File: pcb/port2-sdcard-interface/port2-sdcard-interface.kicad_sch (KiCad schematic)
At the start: 55 parts, among them J2 P2000T Port 2, J3 SD Card, U1 CY62128ELL-45SXI, U10 74HC32, U11 74HC273, U12 74HC165, U13 74HC595, U14 74HC00, U15 SST39SF010, U17 74HC138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

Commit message: LEDs and improved SD card assembly rountines (#2)
* Adding secondary LEDs

* Fixing bug in erroneously triggered LEDs

* Fixing bug in RAM/ROM leds

* Update config.h

* Adding LEDs in software and improvSD card assembly routines
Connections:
- net ~{RD}: no longer U9.5
- net ~{S2}: no longer U9.4
- net ~{S5}: now also U9.4; no longer U4.12, U4.13
- net ~{WR}: now also U9.5
- net at U9.6: now also U4.12, U4.13
- no-connect marks 27 -> 26
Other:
- moved on the sheet: U4D, U9B
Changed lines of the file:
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@@
   (title_block
     (title "Philips P2000T SD-CARD SLOT2 cartridge")
-    (date "2024-01-21")
-    (rev "rev1")
+    (date "2024-03-25")
+    (rev "rev3")
   )
     (symbol "Device:C" (pin_numbers hide) (pin_names (offset 0.254)) (in_bom yes) (on_board yes)
@@
     )
   )
-  (junction (at 142.875 146.685) (diameter 0) (color 0 0 0 0)
-  )
   (junction (at 48.895 203.835) (diameter 0) (color 0 0 0 0)
   )
@@
   (junction (at 35.56 222.885) (diameter 0) (color 0 0 0 0)
   )
+  (junction (at 148.59 149.86) (diameter 0) (color 0 0 0 0)
+  )
   (junction (at 90.17 203.835) (diameter 0) (color 0 0 0 0)
   )
@@
   (no_connect (at 92.71 149.86))
   (no_connect (at 50.165 111.76))
-  (no_connect (at 127 104.14))
   (no_connect (at 50.165 114.3))
   (no_connect (at 90.17 41.275))
@@
     (stroke (width 0) (type default))
   )
-  (wire (pts (xy 142.875 144.145) (xy 142.875 146.685))
-    (stroke (width 0) (type default))
-  )
   (wire (pts (xy 217.678 164.973) (xy 227.457 164.973))
     (stroke (width 0) (type default))
@@
     (stroke (width 0) (type default))
   )
+  (wire (pts (xy 148.59 149.86) (xy 148.59 147.32))
+    (stroke (width 0) (type default))
+  )
   (wire (pts (xy 114.935 53.975) (xy 114.935 56.515))
     (stroke (width 0) (type default))
@@
     (stroke (width 0) (type default))
   )
-  (wire (pts (xy 142.875 146.685) (xy 142.875 149.225))
-    (stroke (width 0) (type default))
-  )
   (wire (pts (xy 287.655 161.925) (xy 301.625 161.925))
     (stroke (width 0) (type default))
@@
     (stroke (width 0) (type default))
   )
+  (wire (pts (xy 148.59 149.86) (xy 148.59 152.4))
+    (stroke (width 0) (type default))
+  )
   (wire (pts (xy 288.925 43.815) (xy 290.83 43.815))
     (stroke (width 0) (type default))
@@
     (stroke (width 0) (type default))
   )
+  (wire (pts (xy 145.415 149.86) (xy 148.59 149.86))
+    (stroke (width 0) (type default))
+  )
   (wire (pts (xy 270.51 41.275) (xy 273.685 41.275))
     (stroke (width 0) (type default))
@@
     (stroke (width 0) (type default))
   )
-  (wire (pts (xy 140.335 146.685) (xy 142.875 146.685))
-    (stroke (width 0) (type default))
-  )
   (wire (pts (xy 288.925 144.145) (xy 288.925 141.605))
     (stroke (width 0) (type default))
@@
     )
   )
+  (global_label "~{WR}" (shape input) (at 130.175 152.4 180) (fields_autoplaced)
+    (effects (font (size 0.9906 0.9906)) (justify right))
+    (property "Intersheetrefs" "${INTERSHEET_REFS}" (at -41.91 305.435 0)
+      (effects (font (size 1.27 1.27)) hide)
+    )
+  )
   (global_label "~{RD}" (shape input) (at 142.875 93.345 180) (fields_autoplaced)
     (effects (font (size 0.9906 0.9906)) (justify right))
@@
     )
   )
-  (global_label "LED_SEL" (shape input) (at 158.115 146.685 0) (fields_autoplaced)
-    (effects (font (size 1 1)) (justify left))
-    (property "Intersheetrefs" "${INTERSHEET_REFS}" (at 166.6082 146.685 0)
-      (effects (font (size 1 1)) (justify left) hide)
-    )
-  )
   (global_label "D4" (shape input) (at 296.545 199.39 180) (fields_autoplaced)
     (effects (font (size 1.27 1.27)) (justify right))
@@
     )
   )
+  (global_label "LED_SEL" (shape input) (at 163.83 149.86 0) (fields_autoplaced)
+    (effects (font (size 1 1)) (justify left))
+    (property "Intersheetrefs" "${INTERSHEET_REFS}" (at 172.3232 149.86 0)
+      (effects (font (size 1 1)) (justify left) hide)
+    )
+  )
   (global_label "D4" (shape input) (at 241.3 261.62 270) (fields_autoplaced)
     (effects (font (size 1.27 1.27)) (justify right))
@@
     )
   )
-  (global_label "~{S2}" (shape input) (at 111.76 101.6 180) (fields_autoplaced)
-    (effects (font (size 1 1)) (justify right))
-    (property "Intersheetrefs" "${INTERSHEET_REFS}" (at 107.9552 101.6625 0)
-      (effects (font (size 1 1)) (justify right) hide)
-    )
-  )
   (global_label "D1" (shape input) (at 296.545 191.77 180) (fields_autoplaced)
     (effects (font (size 1.27 1.27)) (justify right))
@@
     )
   )
-  (global_label "~{RD}" (shape input) (at 111.76 106.68 180) (fields_autoplaced)
-    (effects (font (size 0.9906 0.9906)) (justify right))
-    (property "Intersheetrefs" "${INTERSHEET_REFS}" (at 296.545 -36.195 0)
-      (effects (font (size 1.27 1.27)) hide)
-    )
-  )
   (global_label "~{S11}" (shape input) (at 92.71 137.16 0) (fields_autoplaced)
     (effects (font (size 1 1)) (justify left))
@@
     )
   )
-  (global_label "~{S5}" (shape input) (at 140.335 146.685 180) (fields_autoplaced)
+  (global_label "~{S5}" (shape input) (at 130.175 147.32 180) (fields_autoplaced)
     (effects (font (size 1 1)) (justify right))
-    (property "Intersheetrefs" "${INTERSHEET_REFS}" (at 136.0799 146.685 0)
+    (property "Intersheetrefs" "${INTERSHEET_REFS}" (at 125.9199 147.32 0)
       (effects (font (size 1 1)) (justify right) hide)
     )
@@
     )
   )
-  (symbol (lib_id "74xx:74LS32") (at 119.38 104.14 0) (unit 2)
+  (symbol (lib_id "74xx:74LS32") (at 137.795 149.86 0) (unit 2)
     (in_bom yes) (on_board yes) (dnp no) (fields_autoplaced)
-    (property "Reference" "U9" (at 119.38 96.6302 0)
+    (property "Reference" "U9" (at 137.795 142.3502 0)
       (effects (font (size 1.27 1.27)))
     )
-    (property "Value" "74HC32" (at 119.38 99.1671 0)
+    (property "Value" "74HC32" (at 137.795 144.8871 0)
       (effects (font (size 1.27 1.27)))
     )
-    (property "Footprint" "Package_SO:SO-14_3.9x8.65mm_P1.27mm" (at 119.38 104.14 0)
+    (property "Footprint" "Package_SO:SO-14_3.9x8.65mm_P1.27mm" (at 137.795 149.86 0)
       (effects (font (size 1.27 1.27)) hide)
     )
-    (property "Datasheet" "http://www.ti.com/lit/gpn/sn74LS32" (at 119.38 104.14 0)
+    (property "Datasheet" "http://www.ti.com/lit/gpn/sn74LS32" (at 137.795 149.86 0)
       (effects (font (size 1.27 1.27)) hide)
     )
@@
     )
   )
-  (symbol (lib_id "74xx:74HC00") (at 150.495 146.685 0) (unit 4)
-    (in_bom yes) (on_board yes) (dnp no) (fields_autoplaced)
-    (property "Reference" "U4" (at 150.495 139.1752 0)
+  (symbol (lib_id "74xx:74HC00") (at 156.21 149.86 0) (unit 4)
+    (in_bom yes) (on_board yes) (dnp no)
+    (property "Reference" "U4" (at 156.21 142.3502 0)
       (effects (font (size 1.27 1.27)))
     )
-    (property "Value" "74HC00" (at 150.495 141.7121 0)
+    (property "Value" "74HC00" (at 156.21 144.8871 0)
       (effects (font (size 1.27 1.27)))
     )
-    (property "Footprint" "Package_SO:SO-14_3.9x8.65mm_P1.27mm" (at 150.495 146.685 0)
+    (property "Footprint" "Package_SO:SO-14_3.9x8.65mm_P1.27mm" (at 156.21 149.86 0)
       (effects (font (size 1.27 1.27)) hide)
     )
-    (property "Datasheet" "http://www.ti.com/lit/gpn/sn74hc00" (at 150.495 146.685 0)
+    (property "Datasheet" "http://www.ti.com/lit/gpn/sn74hc00" (at 156.21 149.86 0)
       (effects (font (size 1.27 1.27)) hide)
     )

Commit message: Revising PCB
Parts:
- D3: value ROM -> READ
- D4: value RAM -> WRITE
- R1, R6, R7: value 510 -> 560
- R2: value 510 -> 0
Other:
- note added: "$64: LED selection"
- note added: "SD CARD"
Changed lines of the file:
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@@
   (title_block
     (title "Philips P2000T SD-CARD SLOT2 cartridge")
-    (date "2024-03-25")
-    (rev "rev3")
+    (date "2024-04-09")
+    (rev "rev4")
   )
     (symbol "Device:C" (pin_numbers hide) (pin_names (offset 0.254)) (in_bom yes) (on_board yes)
@@
     (effects (font (size 1.27 1.27)) (justify left bottom))
   )
+  (text "$64: LED selection" (at 125.73 157.48 0)
+    (effects (font (size 1.27 1.27)) (justify left bottom))
+  )
   (text "SHIFT REGISTER SD -> Z80\nIN REGISTER" (at 177.165 81.915 0)
     (effects (font (size 1.27 1.27)) (justify left bottom))
@@
   )
   (text "Set 16 bit address for the ROM and RAM\nchips. The logic circuitry for the ~{CP}\nsignal uses the remaining gates on the\n74HC04, 74HC00 and 74HC21 chips.\n\n* ~{S5} and ~{WR} both LOW, CP for lower byte ADDR HIGH\n* ~{S6} and ~{WR} both LOW, CP for upper byte ADDR HIGH"
-    (at 179.705 188.595 0)
+    (at 176.53 186.69 0)
     (effects (font (size 1.27 1.27)) (justify left bottom))
   )
@@
     (effects (font (size 1.27 1.27)) (justify left bottom))
   )
+  (text "SD CARD" (at 187.96 241.3 0)
+    (effects (font (size 1.27 1.27)) (justify left bottom))
+  )
   (text "SELECTION COMPONENT" (at 17.145 80.01 0)
     (effects (font (size 1.27 1.27)) (justify left bottom))
@@
     (effects (font (size 1.27 1.27)) (justify left bottom))
   )
-  (text "PORT 2 CARTRIDGE SLOT" (at 229.235 240.665 0)
+  (text "PORT 2 CARTRIDGE SLOT" (at 229.87 241.3 0)
     (effects (font (size 1.27 1.27)) (justify left bottom))
   )
@@
     (effects (font (size 1.27 1.27)) (justify left bottom))
   )
-  (text "Two LEDS show whether the SD card is selected\nvia the CS line and whether signals are sent\nto the SD card. Another two leds show I/O on\nthe RAM and ROM chips."
-    (at 176.022 124.46 0)
+  (text "Two LEDS show whether the SD card is selected via the CS line and \nwhether signals are sent to the SD card. Another two leds show I/O \non the RAM and ROM chips."
+    (at 176.53 123.19 0)
     (effects (font (size 1.27 1.27)) (justify left bottom))
   )
@@
   (symbol (lib_id "Device:LED") (at 238.76 155.448 0) (mirror y) (unit 1)
     (in_bom yes) (on_board yes) (dnp no) (fields_autoplaced)
-    (property "Reference" "D3" (at 240.3475 149.098 0)
+    (property "Reference" "D3" (at 240.3475 149.86 0)
       (effects (font (size 1.27 1.27)))
     )
-    (property "Value" "ROM" (at 240.3475 151.638 0)
+    (property "Value" "READ" (at 240.3475 152.4 0)
       (effects (font (size 1.27 1.27)))
     )
@@
       (effects (font (size 1.27 1.27)))
     )
-    (property "Value" "510" (at 231.14 155.448 90)
+    (property "Value" "560" (at 231.14 155.448 90)
       (effects (font (size 1.27 1.27)))
     )
@@
       (effects (font (size 1.27 1.27)))
     )
-    (property "Value" "510" (at 241.935 131.445 90)
+    (property "Value" "560" (at 241.935 131.445 90)
       (effects (font (size 1.27 1.27)))
     )
@@
       (effects (font (size 1.27 1.27)))
     )
-    (property "Value" "510" (at 242.57 144.78 90)
+    (property "Value" "0" (at 242.57 144.78 90)
       (effects (font (size 1.27 1.27)))
     )
@@
   (symbol (lib_id "Device:LED") (at 238.887 164.973 0) (mirror y) (unit 1)
     (in_bom yes) (on_board yes) (dnp no) (fields_autoplaced)
-    (property "Reference" "D4" (at 240.4745 159.004 0)
+    (property "Reference" "D4" (at 240.4745 158.75 0)
       (effects (font (size 1.27 1.27)))
     )
-    (property "Value" "RAM" (at 240.4745 161.544 0)
+    (property "Value" "WRITE" (at 240.4745 161.29 0)
       (effects (font (size 1.27 1.27)))
     )
@@
       (effects (font (size 1.27 1.27)))
     )
-    (property "Value" "510" (at 231.267 164.973 90)
+    (property "Value" "560" (at 231.267 164.973 90)
       (effects (font (size 1.27 1.27)))
     )

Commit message: Adding 4mm inserts
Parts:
- C1, C10, C11, C12, C13, C14, C15, C16, C17, C18, C19, C2, C22, C3, C4, C5, C6, C7, C8, C9: LCSC Part (none) -> C126469
- C20, C21: LCSC Part (none) -> C525286
- R1, R6, R7: LCSC Part (none) -> C429158
- R3, R4: LCSC Part (none) -> C5159708
- R5: LCSC Part (none) -> C5123594
- U1: LCSC Part (none) -> C2840304
- U10, U9: LCSC Part (none) -> C5632
- U11, U8: LCSC Part (none) -> C131486
- U12: LCSC Part (none) -> C5613
- U13: LCSC Part (none) -> C5947
- U14, U2, U4: LCSC Part (none) -> C699445
- U17, U6: LCSC Part (none) -> C5602
- U18, U3: LCSC Part (none) -> C27597
- U19: LCSC Part (none) -> C5588
- U20: LCSC Part (none) -> C5953
- U5: LCSC Part (none) -> C338758
- U7: LCSC Part (none) -> C5597

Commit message: Changing PCB to also accept SST39SF020 and SST39SF040 chips
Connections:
- net GND: now also U15.1 (NC), U15.30 (NC)
- no-connect marks 26 -> 24
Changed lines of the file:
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@@
   (no_connect (at 92.71 147.32))
   (no_connect (at 314.325 154.305))
-  (no_connect (at 321.31 84.455))
   (no_connect (at 235.585 83.185))
   (no_connect (at 200.025 145.923))
   (no_connect (at 92.71 106.045))
-  (no_connect (at 321.31 81.915))
   (no_connect (at 92.71 149.86))
   (no_connect (at 50.165 111.76))
@@
     )
   )
+  (symbol (lib_id "power:GND") (at 321.31 84.455 270) (unit 1)
+    (in_bom yes) (on_board yes) (dnp no)
+    (property "Reference" "#PWR082" (at 314.96 84.455 0)
+      (effects (font (size 1.27 1.27)) hide)
+    )
+    (property "Value" "GND" (at 314.325 84.455 90)
+      (effects (font (size 1.27 1.27)) (justify left))
+    )
+    (property "Footprint" "" (at 321.31 84.455 0)
+      (effects (font (size 1.27 1.27)) hide)
+    )
+    (property "Datasheet" "" (at 321.31 84.455 0)
+      (effects (font (size 1.27 1.27)) hide)
+    )
+    (pin "1")
+    (instances
+      (project "port2-sdcard-interface"
+        (path "/075aea89-321c-44ba-b0b1-8b82a6b1f518"
+          (reference "#PWR082") (unit 1)
+        )
+      )
+    )
+  )
   (symbol (lib_id "Device:C") (at 28.575 213.36 180) (unit 1)
     (in_bom yes) (on_board yes) (dnp no)
@@
         )
       )
+    )
+  )
+  (symbol (lib_id "power:GND") (at 321.31 81.915 270) (unit 1)
+    (in_bom yes) (on_board yes) (dnp no)
+    (property "Reference" "#PWR081" (at 314.96 81.915 0)
+      (effects (font (size 1.27 1.27)) hide)
+    )
+    (property "Value" "GND" (at 314.325 81.915 90)
+      (effects (font (size 1.27 1.27)) (justify left))
+    )
+    (property "Footprint" "" (at 321.31 81.915 0)
+      (effects (font (size 1.27 1.27)) hide)
+    )
+    (property "Datasheet" "" (at 321.31 81.915 0)
+      (effects (font (size 1.27 1.27)) hide)
+    )
+    (pin "1")
+    (instances
+      (project "port2-sdcard-interface"
+        (path "/075aea89-321c-44ba-b0b1-8b82a6b1f518"
+          (reference "#PWR081") (unit 1)
+        )
+      )

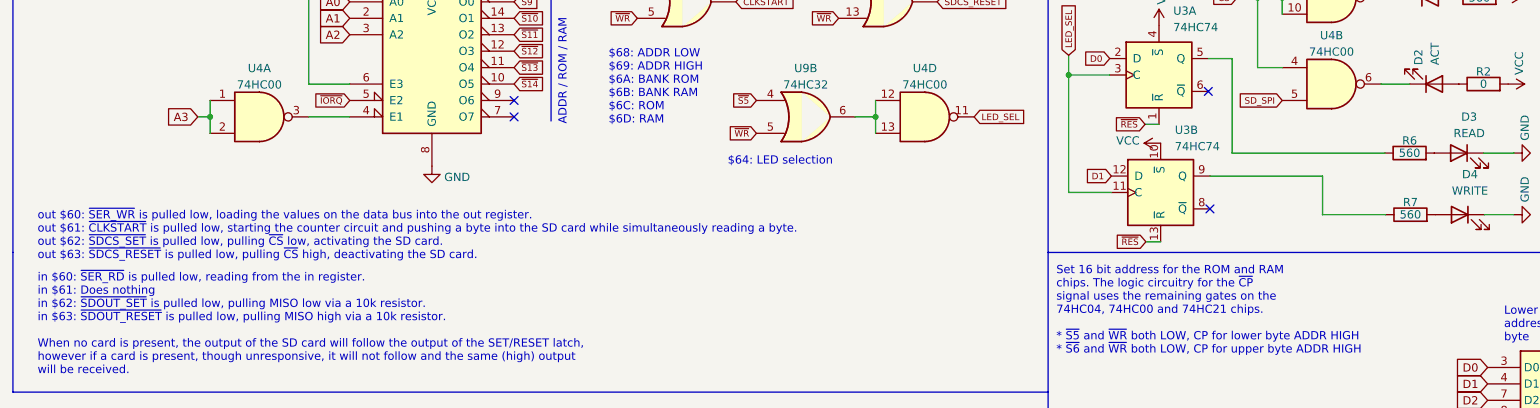
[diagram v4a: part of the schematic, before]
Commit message: Patch 0.4.0 (#5)
* Initial commit retrieving CAS info

* Adding byte replacement function

* Refactoring C to assembly

* Further refactoring SD-card routines

* Further pruning functions and migrating SD card routines to assembly

* Migrating SD card buffer to external RAM and fixing lscas command

* Changing resistor value

* Reintroducing LEDtest and hexdump

* Expanding README

* Adding badges
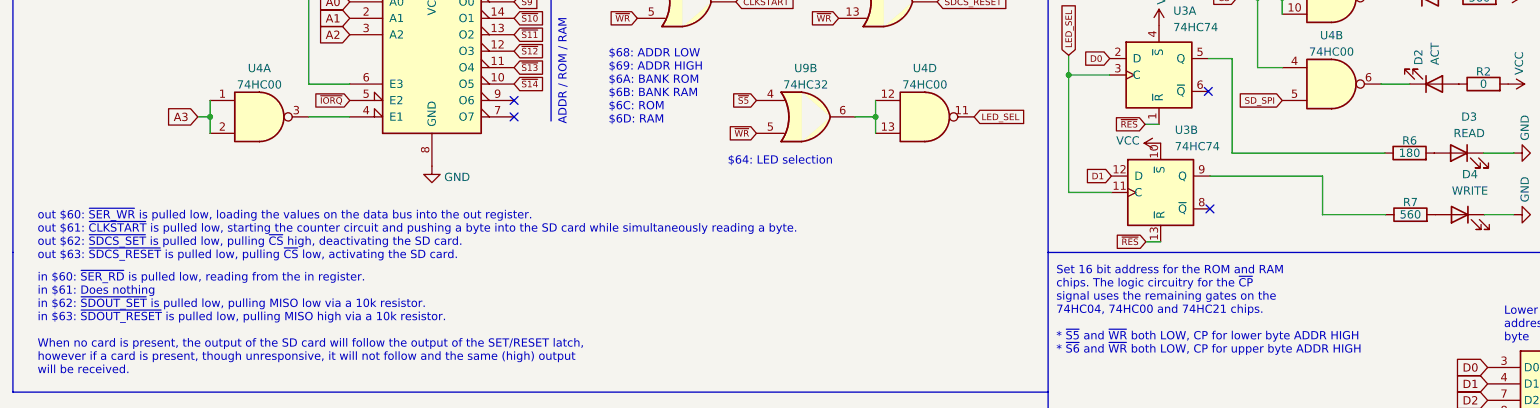
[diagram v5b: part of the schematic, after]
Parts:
- R6: value 560 -> 180
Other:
- note added: "out $60: ~{SER_WR} is pulled low, loading the values on the data bus into the out register. out $61: ~{CLKSTART} is pulled low, starting the counter circuit and pushing a byte into the SD card while simultaneously reading a byte. out $62: ~{SDCS_SET} is pulled low, pulling ~{CS} high, deactivating the SD card. out $63: ~{SDCS_RESET} is pulled low, pulling ~{CS} low, activating the SD card."
- note removed: "out $60: ~{SER_WR} is pulled low, loading the values on the data bus into the out register. out $61: ~{CLKSTART} is pulled low, starting the counter circuit and pushing a byte into the SD card while simultaneously reading a byte. out $62: ~{SDCS_SET} is pulled low, pulling ~{CS} low, activating the SD card. out $63: ~{SDCS_RESET} is pulled low, pulling ~{CS} high, deactivating the SD card."
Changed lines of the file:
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@@
     (effects (font (size 1.27 1.27)) (justify left bottom))
   )
-  (text "out $60: ~{SER_WR} is pulled low, loading the values on the data bus into the out register.\nout $61: ~{CLKSTART} is pulled low, starting the counter circuit and pushing a byte into the SD card while simultaneously reading a byte.\nout $62: ~{SDCS_SET} is pulled low, pulling ~{CS} low, activating the SD card.\nout $63: ~{SDCS_RESET} is pulled low, pulling ~{CS} high, deactivating the SD card."
+  (text "out $60: ~{SER_WR} is pulled low, loading the values on the data bus into the out register.\nout $61: ~{CLKSTART} is pulled low, starting the counter circuit and pushing a byte into the SD card while simultaneously reading a byte.\nout $62: ~{SDCS_SET} is pulled low, pulling ~{CS} high, deactivating the SD card.\nout $63: ~{SDCS_RESET} is pulled low, pulling ~{CS} low, activating the SD card."
     (at 19.05 172.085 0)
     (effects (font (size 1.27 1.27)) (justify left bottom))
@@
       (effects (font (size 1.27 1.27)))
     )
-    (property "Value" "560" (at 231.14 155.448 90)
-      (effects (font (size 1.27 1.27)))
-    )
+    (property "Value" "180" (at 231.14 155.448 90)
+      (effects (font (size 1.27 1.27)))
+    )
